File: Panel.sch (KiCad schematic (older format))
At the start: 11 parts, among them J7 Rotated_Barrel, U7 LM3406HV

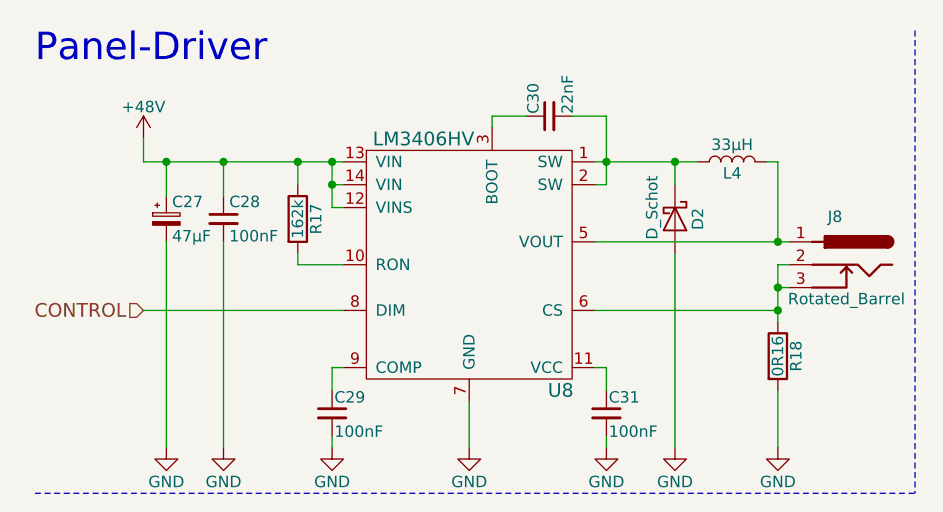
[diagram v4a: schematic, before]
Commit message: Fixed the Panel-Inductor(was too small)
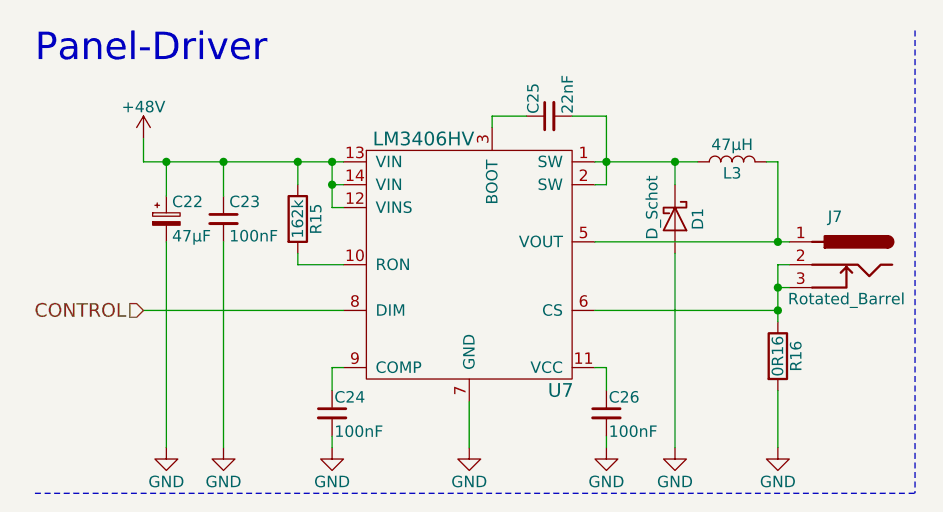
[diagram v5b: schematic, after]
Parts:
- L3: value 33μH -> 47μH; Buy https://www.digikey.com/product-detail/en/taiyo-yuden/NS101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 -> https://www.digikey.com/product-detail/en/bourns-inc/SRR120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
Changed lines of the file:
@@
 $Descr A4 11693 8268
 encoding utf-8
-Sheet 4 7
+Sheet 3 7
 Title ""
 Date "2018-02-14"
@@
 AR Path="/5A4C34AF/5A7753B7" Ref="R15"  Part="1"
 AR Path="/5A4C3F5F/5A7753B7" Ref="R17"  Part="1"
-F 0 "R17" V 1705 1300 50  0000 C CNN
+F 0 "R15" V 1705 1300 50  0000 C CNN
 F 1 "162k" V 1625 1300 50  0000 C CNN
 F 2 "Resistors_SMD:R_0603" V 1555 1300 50  0001 C CNN
@@
 AR Path="/5A4C34AF/5A77745B" Ref="C24"  Part="1"
 AR Path="/5A4C3F5F/5A77745B" Ref="C29"  Part="1"
-F 0 "C29" H 1785 2220 50  0000 L CNN
+F 0 "C24" H 1785 2220 50  0000 L CNN
 F 1 "100nF" H 1785 2070 50  0000 L CNN
 F 2 "Capacitors_SMD:C_0603" H 1775 2150 50  0001 C CNN
@@
 AR Path="/5A4C34AF/5A777BDD" Ref="#PWR063"  Part="1"
 AR Path="/5A4C3F5F/5A777BDD" Ref="#PWR071"  Part="1"
-F 0 "#PWR071" H 1775 2050 50  0001 C CNN
+F 0 "#PWR063" H 1775 2050 50  0001 C CNN
 F 1 "GND" H 1775 2150 50  0000 C CNN
 F 2 "" H 1775 2300 50  0001 C CNN
@@
 AR Path="/5A4C34AF/5A777CD4" Ref="C26"  Part="1"
 AR Path="/5A4C3F5F/5A777CD4" Ref="C31"  Part="1"
-F 0 "C31" H 2985 2220 50  0000 L CNN
+F 0 "C26" H 2985 2220 50  0000 L CNN
 F 1 "100nF" H 2985 2070 50  0000 L CNN
 F 2 "Capacitors_SMD:C_0603" H 2975 2150 50  0001 C CNN
@@
 AR Path="/5A4C34AF/5A777CDA" Ref="#PWR065"  Part="1"
 AR Path="/5A4C3F5F/5A777CDA" Ref="#PWR073"  Part="1"
-F 0 "#PWR073" H 2975 2050 50  0001 C CNN
+F 0 "#PWR065" H 2975 2050 50  0001 C CNN
 F 1 "GND" H 2975 2150 50  0000 C CNN
 F 2 "" H 2975 2300 50  0001 C CNN
@@
 AR Path="/5A4C34AF/5A777FA3" Ref="#PWR064"  Part="1"
 AR Path="/5A4C3F5F/5A777FA3" Ref="#PWR072"  Part="1"
-F 0 "#PWR072" H 2375 2050 50  0001 C CNN
+F 0 "#PWR064" H 2375 2050 50  0001 C CNN
 F 1 "GND" H 2375 2150 50  0000 C CNN
 F 2 "" H 2375 2300 50  0001 C CNN
@@
 AR Path="/5A4C34AF/5A77816D" Ref="C25"  Part="1"
 AR Path="/5A4C3F5F/5A77816D" Ref="C30"  Part="1"
-F 0 "C30" H 2735 920 50  0000 L CNN
+F 0 "C25" H 2735 920 50  0000 L CNN
 F 1 "22nF" H 2735 770 50  0000 L CNN
 F 2 "Capacitors_SMD:C_0603" H 2725 850 50  0001 C CNN
@@
 AR Path="/5A4C34AF/5A77899A" Ref="L3"  Part="1"
 AR Path="/5A4C3F5F/5A77899A" Ref="L4"  Part="1"
-F 0 "L4" V 3475 1050 50  0000 C CNN
-F 1 "33μH" V 3600 1050 50  0000 C CNN
+F 0 "L3" V 3475 1050 50  0000 C CNN
+F 1 "47μH" V 3600 1050 50  0000 C CNN
 F 2 "" H 3525 1050 50  0001 C CNN
 F 3 "" H 3525 1050 50  0001 C CNN
-F 4 "https://www.digikey.com/product-detail/en/taiyo-yuden/NS10145T330MNA/587-3126-1-ND/2774716" V 3525 1050 60  0001 C CNN "Buy"
+F 4 "https://www.digikey.com/product-detail/en/bourns-inc/SRR1208-470YL/SRR1208-470YLCT-ND/2353025" V 3525 1050 60  0001 C CNN "Buy"
 	1    3525 1050
 	0    -1   -1   0
@@
 AR Path="/5A4C34AF/5A7789F9" Ref="D1"  Part="1"
 AR Path="/5A4C3F5F/5A7789F9" Ref="D2"  Part="1"
-F 0 "D2" H 3275 1400 50  0000 C CNN
+F 0 "D1" H 3275 1400 50  0000 C CNN
 F 1 "D_Schot" H 3225 1200 50  0000 C CNN
 F 2 "Diode_SMD:D_SMA_Handsoldering" H 3275 1300 50  0001 C CNN
@@
 AR Path="/5A4C34AF/5A778B62" Ref="#PWR066"  Part="1"
 AR Path="/5A4C3F5F/5A778B62" Ref="#PWR074"  Part="1"
-F 0 "#PWR074" H 3275 2050 50  0001 C CNN
+F 0 "#PWR066" H 3275 2050 50  0001 C CNN
 F 1 "GND" H 3275 2150 50  0000 C CNN
 F 2 "" H 3275 2300 50  0001 C CNN
@@
 AR Path="/5A4C34AF/5A779AD3" Ref="J7"  Part="1"
 AR Path="/5A4C3F5F/5A779AD3" Ref="J8"  Part="1"
-F 0 "J8" H 3975 1710 50  0000 C CNN
+F 0 "J7" H 3975 1710 50  0000 C CNN
 F 1 "Rotated_Barrel" H 4025 1350 50  0000 C CNN
 F 2 "Connectors:BARREL_JACK" H 4025 1440 50  0001 C CNN
@@
 AR Path="/5A4C34AF/5A77A2E1" Ref="R16"  Part="1"
 AR Path="/5A4C3F5F/5A77A2E1" Ref="R18"  Part="1"
-F 0 "R18" V 3805 1900 50  0000 C CNN
+F 0 "R16" V 3805 1900 50  0000 C CNN
 F 1 "0R16" V 3725 1900 50  0000 C CNN
 F 2 "Resistors_SMD:R_0805" V 3655 1900 50  0001 C CNN
@@
 AR Path="/5A4C34AF/5A77A9CB" Ref="#PWR067"  Part="1"
 AR Path="/5A4C3F5F/5A77A9CB" Ref="#PWR075"  Part="1"
-F 0 "#PWR075" H 3725 2050 50  0001 C CNN
+F 0 "#PWR067" H 3725 2050 50  0001 C CNN
 F 1 "GND" H 3725 2150 50  0000 C CNN
 F 2 "" H 3725 2300 50  0001 C CNN
@@
 AR Path="/5A4C34AF/5A77D43C" Ref="#PWR062"  Part="1"
 AR Path="/5A4C3F5F/5A77D43C" Ref="#PWR070"  Part="1"
-F 0 "#PWR070" H 1300 2050 50  0001 C CNN
+F 0 "#PWR062" H 1300 2050 50  0001 C CNN
 F 1 "GND" H 1300 2150 50  0000 C CNN
 F 2 "" H 1300 2300 50  0001 C CNN
@@
 AR Path="/5A4C34AF/5A77E620" Ref="U7"  Part="1"
 AR Path="/5A4C3F5F/5A77E620" Ref="U8"  Part="1"
-F 0 "U8" H 2775 950 60  0000 C CNN
+F 0 "U7" H 2775 950 60  0000 C CNN
 F 1 "LM3406HV" H 2175 2050 60  0000 C CNN
 F 2 "Housings_SSOP:TSSOP-14_4.4x5mm_Pitch0.65mm" H 2375 2100 60  0001 C CNN
@@
 AR Path="/5A4C34AF/5A84C99A" Ref="#PWR060"  Part="1"
 AR Path="/5A4C3F5F/5A84C99A" Ref="#PWR068"  Part="1"
-F 0 "#PWR068" H 950 800 50  0001 C CNN
+F 0 "#PWR060" H 950 800 50  0001 C CNN
 F 1 "+48V" H 950 1090 50  0000 C CNN
 F 2 "" H 950 950 50  0001 C CNN
@@
 AR Path="/5A4C34AF/5ABA3DDA" Ref="C22"  Part="1"
 AR Path="/5A4C3F5F/5ABA3DDA" Ref="C27"  Part="1"
-F 0 "C27" H 1075 1375 50  0000 L CNN
+F 0 "C22" H 1075 1375 50  0000 L CNN
 F 1 "47μF" H 1075 1225 50  0000 L CNN
 F 2 "" H 1050 1300 50  0001 C CNN
@@
 AR Path="/5A4C34AF/5ABA5E6C" Ref="C23"  Part="1"
 AR Path="/5A4C3F5F/5ABA5E6C" Ref="C28"  Part="1"
-F 0 "C28" H 1325 1375 50  0000 L CNN
+F 0 "C23" H 1325 1375 50  0000 L CNN
 F 1 "100nF" H 1325 1225 50  0000 L CNN
 F 2 "Capacitor_SMD:C_0805_2012Metric" H 1300 1300 50  0001 C CNN
@@
 AR Path="/5A4C34AF/5ABA815F" Ref="#PWR061"  Part="1"
 AR Path="/5A4C3F5F/5ABA815F" Ref="#PWR069"  Part="1"
-F 0 "#PWR069" H 1050 2050 50  0001 C CNN
+F 0 "#PWR061" H 1050 2050 50  0001 C CNN
 F 1 "GND" H 1050 2150 50  0000 C CNN
 F 2 "" H 1050 2300 50  0001 C CNN

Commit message: Switch to new kicad footprint library
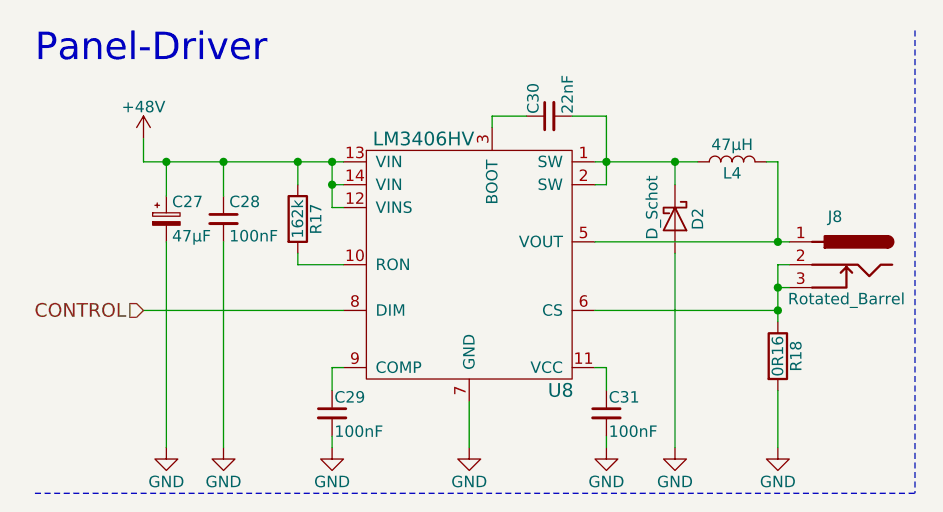
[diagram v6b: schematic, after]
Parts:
- C24, C25, C26: footprint Capacitors_SMD:C_0603 -> Capacitor_SMD:C_0603_1608Metric
- J7: footprint Connectors:BARREL_JACK -> (none)
- R15: footprint Resistors_SMD:R_0603 -> Resistor_SMD:R_0603_1608Metric
- R16: footprint Resistors_SMD:R_0805 -> Resistor_SMD:R_0805_2012Metric
- U7: footprint Housings_SSOP:TSSOP-14_4.4x5mm_Pitch0.65mm -> Package_SO:TSSOP-14_4.4x5mm_P0.65mm
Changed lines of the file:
@@
 AR Path="/5A4C34AF/5A7753B7" Ref="R15"  Part="1"
 AR Path="/5A4C3F5F/5A7753B7" Ref="R17"  Part="1"
-F 0 "R15" V 1705 1300 50  0000 C CNN
+F 0 "R17" V 1705 1300 50  0000 C CNN
 F 1 "162k" V 1625 1300 50  0000 C CNN
-F 2 "Resistors_SMD:R_0603" V 1555 1300 50  0001 C CNN
+F 2 "Resistor_SMD:R_0603_1608Metric" V 1555 1300 50  0001 C CNN
 F 3 "" H 1625 1300 50  0001 C CNN
 F 4 "https://www.digikey.com/product-detail/en/yageo/RC0603FR-07162KL/311-162KHRCT-ND/729922" V 1625 1300 50  0001 C CNN "Buy"
@@
 AR Path="/5A4C34AF/5A77745B" Ref="C24"  Part="1"
 AR Path="/5A4C3F5F/5A77745B" Ref="C29"  Part="1"
-F 0 "C24" H 1785 2220 50  0000 L CNN
+F 0 "C29" H 1785 2220 50  0000 L CNN
 F 1 "100nF" H 1785 2070 50  0000 L CNN
-F 2 "Capacitors_SMD:C_0603" H 1775 2150 50  0001 C CNN
+F 2 "Capacitor_SMD:C_0603_1608Metric" H 1775 2150 50  0001 C CNN
 F 3 "" H 1775 2150 50  0001 C CNN
 F 4 "https://www.digikey.com/product-detail/en/kemet/C0603C104K3RACTU/399-1281-1-ND/416057" H 1775 2150 60  0001 C CNN "Buy"
@@
 AR Path="/5A4C34AF/5A777BDD" Ref="#PWR063"  Part="1"
 AR Path="/5A4C3F5F/5A777BDD" Ref="#PWR071"  Part="1"
-F 0 "#PWR063" H 1775 2050 50  0001 C CNN
+F 0 "#PWR071" H 1775 2050 50  0001 C CNN
 F 1 "GND" H 1775 2150 50  0000 C CNN
 F 2 "" H 1775 2300 50  0001 C CNN
@@
 AR Path="/5A4C34AF/5A777CD4" Ref="C26"  Part="1"
 AR Path="/5A4C3F5F/5A777CD4" Ref="C31"  Part="1"
-F 0 "C26" H 2985 2220 50  0000 L CNN
+F 0 "C31" H 2985 2220 50  0000 L CNN
 F 1 "100nF" H 2985 2070 50  0000 L CNN
-F 2 "Capacitors_SMD:C_0603" H 2975 2150 50  0001 C CNN
+F 2 "Capacitor_SMD:C_0603_1608Metric" H 2975 2150 50  0001 C CNN
 F 3 "" H 2975 2150 50  0001 C CNN
 F 4 "https://www.digikey.com/product-detail/en/kemet/C0603C104K3RACTU/399-1281-1-ND/416057" H 2975 2150 50  0001 C CNN "Buy"
@@
 AR Path="/5A4C34AF/5A777CDA" Ref="#PWR065"  Part="1"
 AR Path="/5A4C3F5F/5A777CDA" Ref="#PWR073"  Part="1"
-F 0 "#PWR065" H 2975 2050 50  0001 C CNN
+F 0 "#PWR073" H 2975 2050 50  0001 C CNN
 F 1 "GND" H 2975 2150 50  0000 C CNN
 F 2 "" H 2975 2300 50  0001 C CNN
@@
 AR Path="/5A4C34AF/5A777FA3" Ref="#PWR064"  Part="1"
 AR Path="/5A4C3F5F/5A777FA3" Ref="#PWR072"  Part="1"
-F 0 "#PWR064" H 2375 2050 50  0001 C CNN
+F 0 "#PWR072" H 2375 2050 50  0001 C CNN
 F 1 "GND" H 2375 2150 50  0000 C CNN
 F 2 "" H 2375 2300 50  0001 C CNN
@@
 AR Path="/5A4C34AF/5A77816D" Ref="C25"  Part="1"
 AR Path="/5A4C3F5F/5A77816D" Ref="C30"  Part="1"
-F 0 "C25" H 2735 920 50  0000 L CNN
+F 0 "C30" H 2735 920 50  0000 L CNN
 F 1 "22nF" H 2735 770 50  0000 L CNN
-F 2 "Capacitors_SMD:C_0603" H 2725 850 50  0001 C CNN
+F 2 "Capacitor_SMD:C_0603_1608Metric" H 2725 850 50  0001 C CNN
 F 3 "" H 2725 850 50  0001 C CNN
 F 4 "https://www.digikey.com/product-detail/en/kemet/C0603C223K1RACTU/399-3476-1-ND/754769" H 2725 850 50  0001 C CNN "Buy"
@@
 AR Path="/5A4C34AF/5A77899A" Ref="L3"  Part="1"
 AR Path="/5A4C3F5F/5A77899A" Ref="L4"  Part="1"
-F 0 "L3" V 3475 1050 50  0000 C CNN
+F 0 "L4" V 3475 1050 50  0000 C CNN
 F 1 "47μH" V 3600 1050 50  0000 C CNN
 F 2 "" H 3525 1050 50  0001 C CNN
@@
 AR Path="/5A4C34AF/5A7789F9" Ref="D1"  Part="1"
 AR Path="/5A4C3F5F/5A7789F9" Ref="D2"  Part="1"
-F 0 "D1" H 3275 1400 50  0000 C CNN
+F 0 "D2" H 3275 1400 50  0000 C CNN
 F 1 "D_Schot" H 3225 1200 50  0000 C CNN
 F 2 "Diode_SMD:D_SMA_Handsoldering" H 3275 1300 50  0001 C CNN
@@
 AR Path="/5A4C34AF/5A778B62" Ref="#PWR066"  Part="1"
 AR Path="/5A4C3F5F/5A778B62" Ref="#PWR074"  Part="1"
-F 0 "#PWR066" H 3275 2050 50  0001 C CNN
+F 0 "#PWR074" H 3275 2050 50  0001 C CNN
 F 1 "GND" H 3275 2150 50  0000 C CNN
 F 2 "" H 3275 2300 50  0001 C CNN
@@
 AR Path="/5A4C34AF/5A779AD3" Ref="J7"  Part="1"
 AR Path="/5A4C3F5F/5A779AD3" Ref="J8"  Part="1"
-F 0 "J7" H 3975 1710 50  0000 C CNN
+F 0 "J8" H 3975 1710 50  0000 C CNN
 F 1 "Rotated_Barrel" H 4025 1350 50  0000 C CNN
-F 2 "Connectors:BARREL_JACK" H 4025 1440 50  0001 C CNN
+F 2 "" H 4025 1440 50  0001 C CNN
 F 3 "" H 4025 1440 50  0001 C CNN
 	1    3975 1500
@@
 AR Path="/5A4C34AF/5A77A2E1" Ref="R16"  Part="1"
 AR Path="/5A4C3F5F/5A77A2E1" Ref="R18"  Part="1"
-F 0 "R16" V 3805 1900 50  0000 C CNN
+F 0 "R18" V 3805 1900 50  0000 C CNN
 F 1 "0R16" V 3725 1900 50  0000 C CNN
-F 2 "Resistors_SMD:R_0805" V 3655 1900 50  0001 C CNN
+F 2 "Resistor_SMD:R_0805_2012Metric" V 3655 1900 50  0001 C CNN
 F 3 "" H 3725 1900 50  0001 C CNN
 F 4 "https://www.digikey.com/product-detail/en/panasonic-electronic-components/ERJ-6DSFR16V/P19313CT-ND/6004668" V 3725 1900 60  0001 C CNN "Buy"
@@
 AR Path="/5A4C34AF/5A77A9CB" Ref="#PWR067"  Part="1"
 AR Path="/5A4C3F5F/5A77A9CB" Ref="#PWR075"  Part="1"
-F 0 "#PWR067" H 3725 2050 50  0001 C CNN
+F 0 "#PWR075" H 3725 2050 50  0001 C CNN
 F 1 "GND" H 3725 2150 50  0000 C CNN
 F 2 "" H 3725 2300 50  0001 C CNN
@@
 AR Path="/5A4C34AF/5A77D43C" Ref="#PWR062"  Part="1"
 AR Path="/5A4C3F5F/5A77D43C" Ref="#PWR070"  Part="1"
-F 0 "#PWR062" H 1300 2050 50  0001 C CNN
+F 0 "#PWR070" H 1300 2050 50  0001 C CNN
 F 1 "GND" H 1300 2150 50  0000 C CNN
 F 2 "" H 1300 2300 50  0001 C CNN
@@
 AR Path="/5A4C34AF/5A77E620" Ref="U7"  Part="1"
 AR Path="/5A4C3F5F/5A77E620" Ref="U8"  Part="1"
-F 0 "U7" H 2775 950 60  0000 C CNN
+F 0 "U8" H 2775 950 60  0000 C CNN
 F 1 "LM3406HV" H 2175 2050 60  0000 C CNN
-F 2 "Housings_SSOP:TSSOP-14_4.4x5mm_Pitch0.65mm" H 2375 2100 60  0001 C CNN
+F 2 "Package_SO:TSSOP-14_4.4x5mm_P0.65mm" H 2375 2100 60  0001 C CNN
 F 3 "http://www.ti.com/lit/ds/symlink/lm3406.pdf" H 2375 2100 60  0001 C CNN
 F 4 "https://www.digikey.com/product-detail/en/texas-instruments/LM3406HVMHX-NOPB/LM3406HVMHX-NOPBCT-ND/3526958" H 2375 1500 60  0001 C CNN "Buy"
@@
 AR Path="/5A4C34AF/5A84C99A" Ref="#PWR060"  Part="1"
 AR Path="/5A4C3F5F/5A84C99A" Ref="#PWR068"  Part="1"
-F 0 "#PWR060" H 950 800 50  0001 C CNN
+F 0 "#PWR068" H 950 800 50  0001 C CNN
 F 1 "+48V" H 950 1090 50  0000 C CNN
 F 2 "" H 950 950 50  0001 C CNN
@@
 AR Path="/5A4C34AF/5ABA3DDA" Ref="C22"  Part="1"
 AR Path="/5A4C3F5F/5ABA3DDA" Ref="C27"  Part="1"
-F 0 "C22" H 1075 1375 50  0000 L CNN
+F 0 "C27" H 1075 1375 50  0000 L CNN
 F 1 "47μF" H 1075 1225 50  0000 L CNN
 F 2 "" H 1050 1300 50  0001 C CNN
@@
 AR Path="/5A4C34AF/5ABA5E6C" Ref="C23"  Part="1"
 AR Path="/5A4C3F5F/5ABA5E6C" Ref="C28"  Part="1"
-F 0 "C23" H 1325 1375 50  0000 L CNN
+F 0 "C28" H 1325 1375 50  0000 L CNN
 F 1 "100nF" H 1325 1225 50  0000 L CNN
 F 2 "Capacitor_SMD:C_0805_2012Metric" H 1300 1300 50  0001 C CNN
@@
 AR Path="/5A4C34AF/5ABA815F" Ref="#PWR061"  Part="1"
 AR Path="/5A4C3F5F/5ABA815F" Ref="#PWR069"  Part="1"
-F 0 "#PWR061" H 1050 2050 50  0001 C CNN
+F 0 "#PWR069" H 1050 2050 50  0001 C CNN
 F 1 "GND" H 1050 2150 50  0000 C CNN
 F 2 "" H 1050 2300 50  0001 C CNN

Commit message: Replaced the 100nF Low-Voltage-Caps with one, which is still in stock
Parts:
- C24, C26: Buy https://www.digikey.com/product-detail/en/kemet/C0603C104K3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 -> https://www.digikey.com/product-detail/en/murata-electronic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
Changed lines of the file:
@@
 F 2 "Capacitor_SMD:C_0603_1608Metric" H 1775 2150 50  0001 C CNN
 F 3 "" H 1775 2150 50  0001 C CNN
-F 4 "https://www.digikey.com/product-detail/en/kemet/C0603C104K3RACTU/399-1281-1-ND/416057" H 1775 2150 60  0001 C CNN "Buy"
+F 4 "https://www.digikey.com/product-detail/en/murata-electronics-north-america/GCM188R71C104KA37D/490-4774-1-ND/1641693" H 1775 2150 60  0001 C CNN "Buy"
 	1    1775 2150
 	1    0    0    -1
@@
 F 2 "Capacitor_SMD:C_0603_1608Metric" H 2975 2150 50  0001 C CNN
 F 3 "" H 2975 2150 50  0001 C CNN
-F 4 "https://www.digikey.com/product-detail/en/kemet/C0603C104K3RACTU/399-1281-1-ND/416057" H 2975 2150 50  0001 C CNN "Buy"
+F 4 "https://www.digikey.com/product-detail/en/murata-electronics-north-america/GCM188R71C104KA37D/490-4774-1-ND/1641693" H 2975 2150 50  0001 C CNN "Buy"
 	1    2975 2150
 	1    0    0    -1
